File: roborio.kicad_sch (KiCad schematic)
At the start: 0 parts

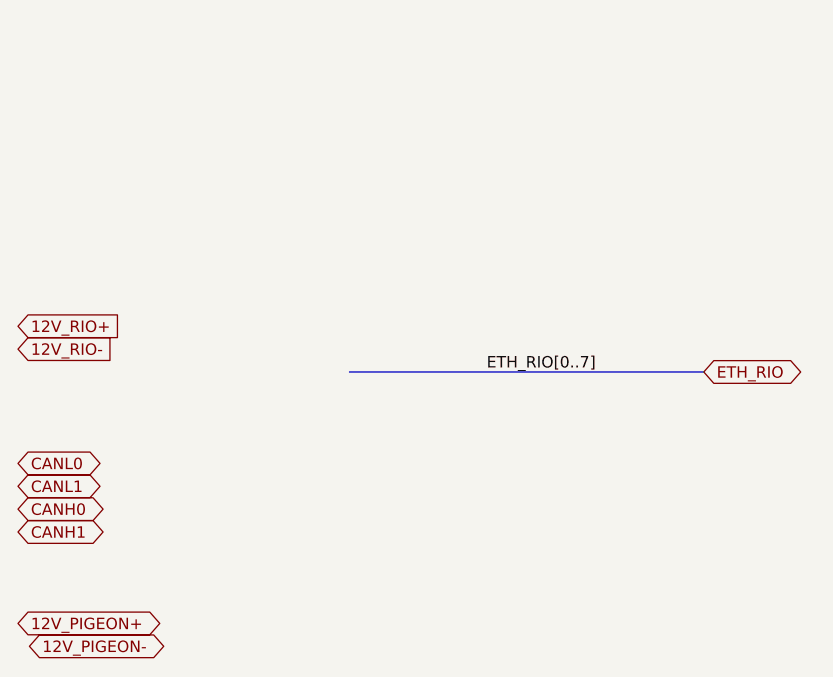
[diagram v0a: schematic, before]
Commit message: Jonathan: Completed roborio, swerve, and top level schematics Added and wired radio
Jeremy:
Fixed unnamed radio file

Signed-off-by: Jeremy Siegfried <jeremy.siegfried@howlandschools.org>
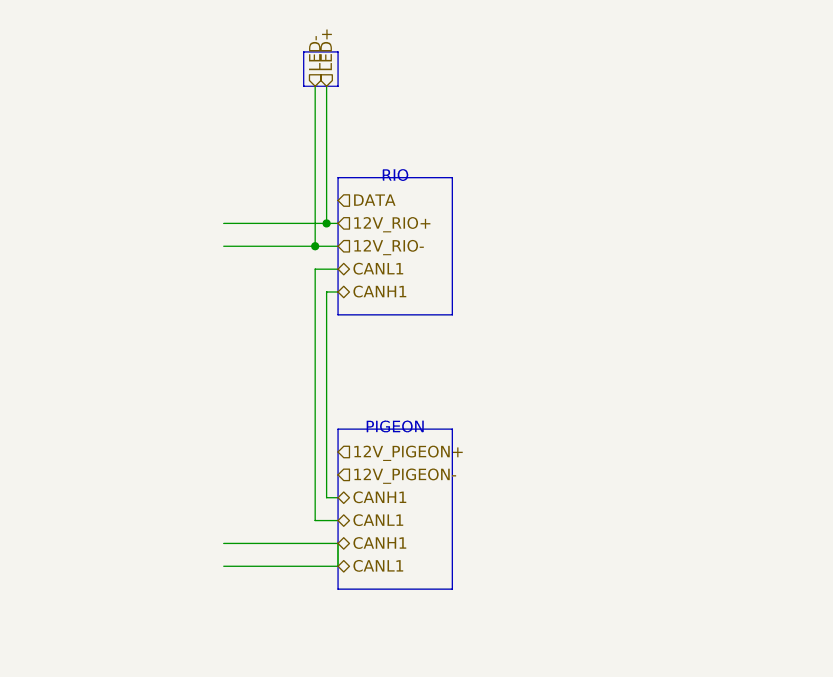
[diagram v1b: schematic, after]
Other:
- note added: "PIGEON"
- note added: "RIO"
